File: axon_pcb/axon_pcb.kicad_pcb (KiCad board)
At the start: 2 copper layers, 227.6 x 99.2 mm, 120 parts, among them J1 USB_C_Receptacle, J2 AVR_ISP Header, K1 KEYSW, K10 KEYSW, K11 KEYSW, K12 KEYSW, K13 KEYSW, K14 KEYSW, K15 KEYSW, K16 KEYSW, K17 KEYSW, K18 KEYSW, K19 KEYSW, K2 KEYSW, K20 KEYSW, K21 KEYSW, K22 KEYSW, K23 KEYSW, K24 KEYSW, K25 KEYSW, K26 KEYSW, K27 KEYSW, K28 KEYSW, K29 KEYSW, K3 KEYSW, K30 KEYSW, K31 KEYSW, K32 KEYSW, K33 KEYSW, K34 KEYSW, K35 KEYSW, K36 KEYSW, K37 KEYSW, K38 KEYSW, K39 KEYSW, K4 KEYSW, K40 KEYSW, K41 KEYSW, K42 KEYSW, K5 KEYSW, K6 KEYSW, K7 KEYSW, K8 KEYSW, K9 KEYSW, SW1 RESET, SW2 BOOT, U1 ATmega328P-PU, X1 16MHz

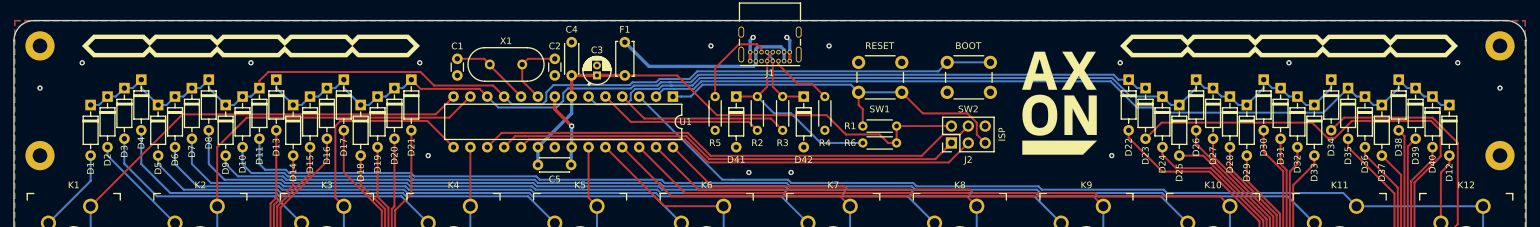
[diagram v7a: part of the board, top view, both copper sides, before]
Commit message: update board: acrylic fastener symmetry and elec cap placement
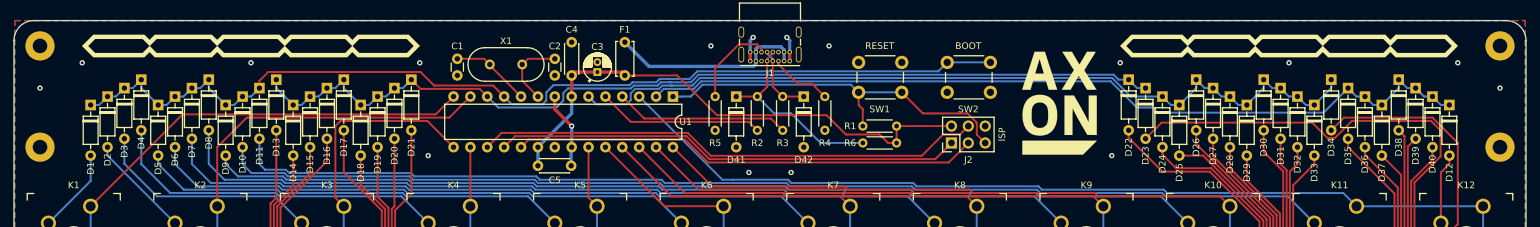
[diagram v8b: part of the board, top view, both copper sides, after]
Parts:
- moved REF** 1.27 mm to (-5.08, -14.0)
- moved REF** 1.27 mm to (214.6, -14.0)
- moved C3 0.51 mm to (78.8, -25.3)
- moved C5 0.13 mm to (69.8, -11.2)
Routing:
- net +5V: track 79.5 -> 80.0 mm
